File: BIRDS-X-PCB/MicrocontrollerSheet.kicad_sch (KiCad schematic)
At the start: 10 parts, among them J401 Conn_02x04_Odd_Even, J402 Conn_01x08, SW401 SW_Push, U401 STM32G031K8Tx, U402 MTT4B-Mini, U403 MT29F2G01ABAGDWB-IT-G_TR, Y401 ECS-2520SMV-080-FN-TR

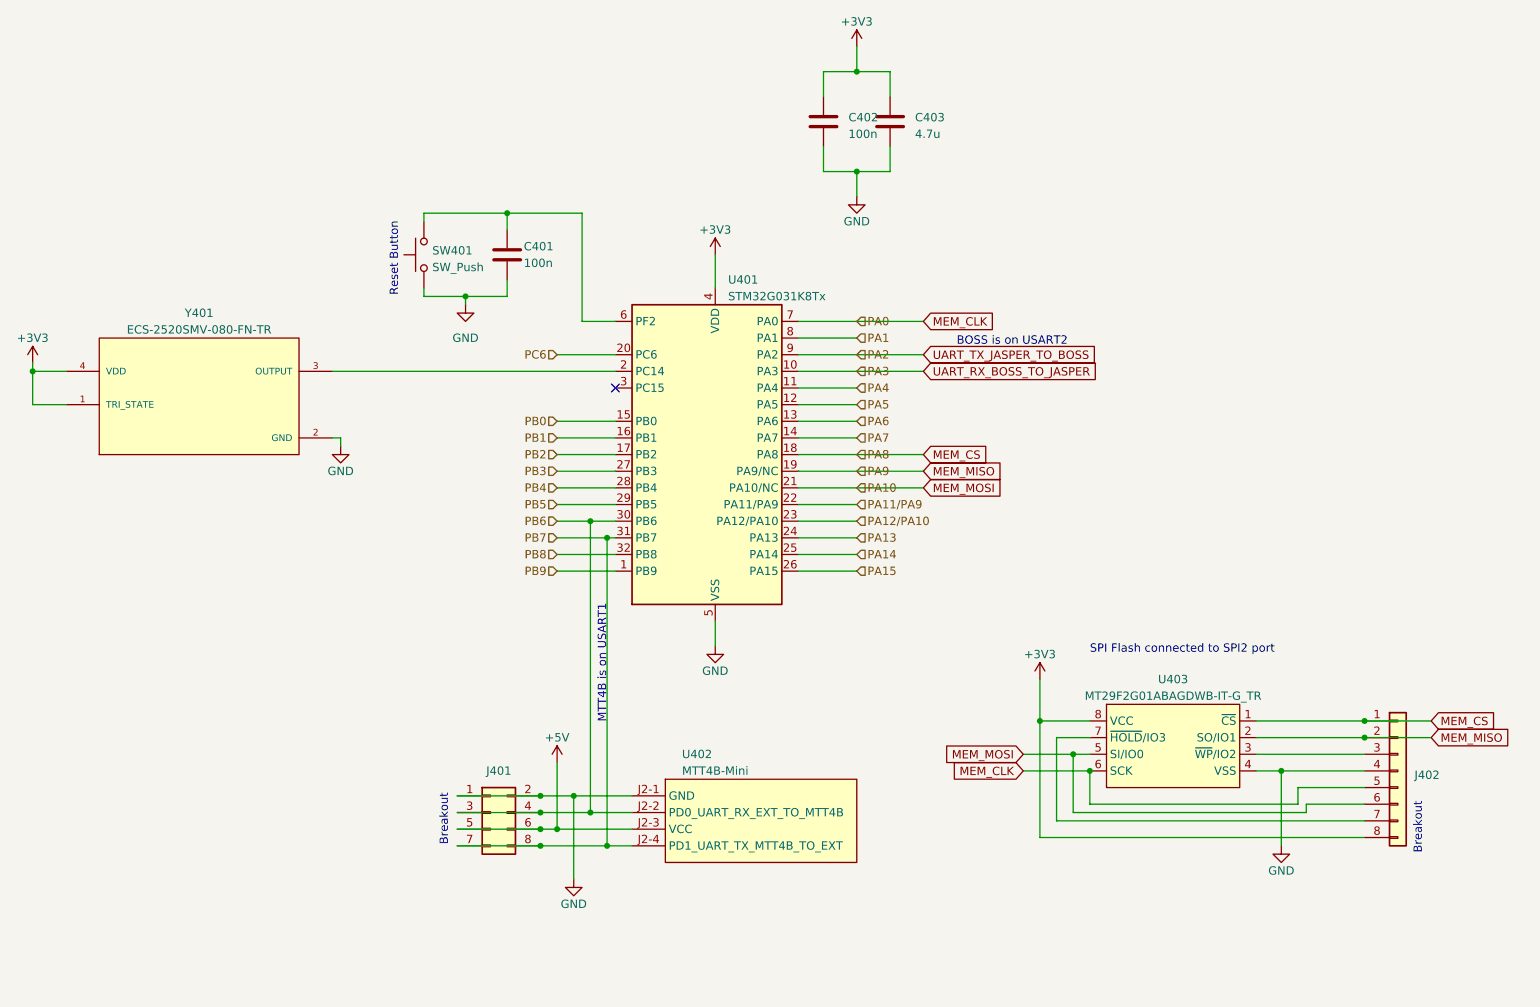
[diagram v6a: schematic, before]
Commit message: Semantic and symbol updates, begin review changes
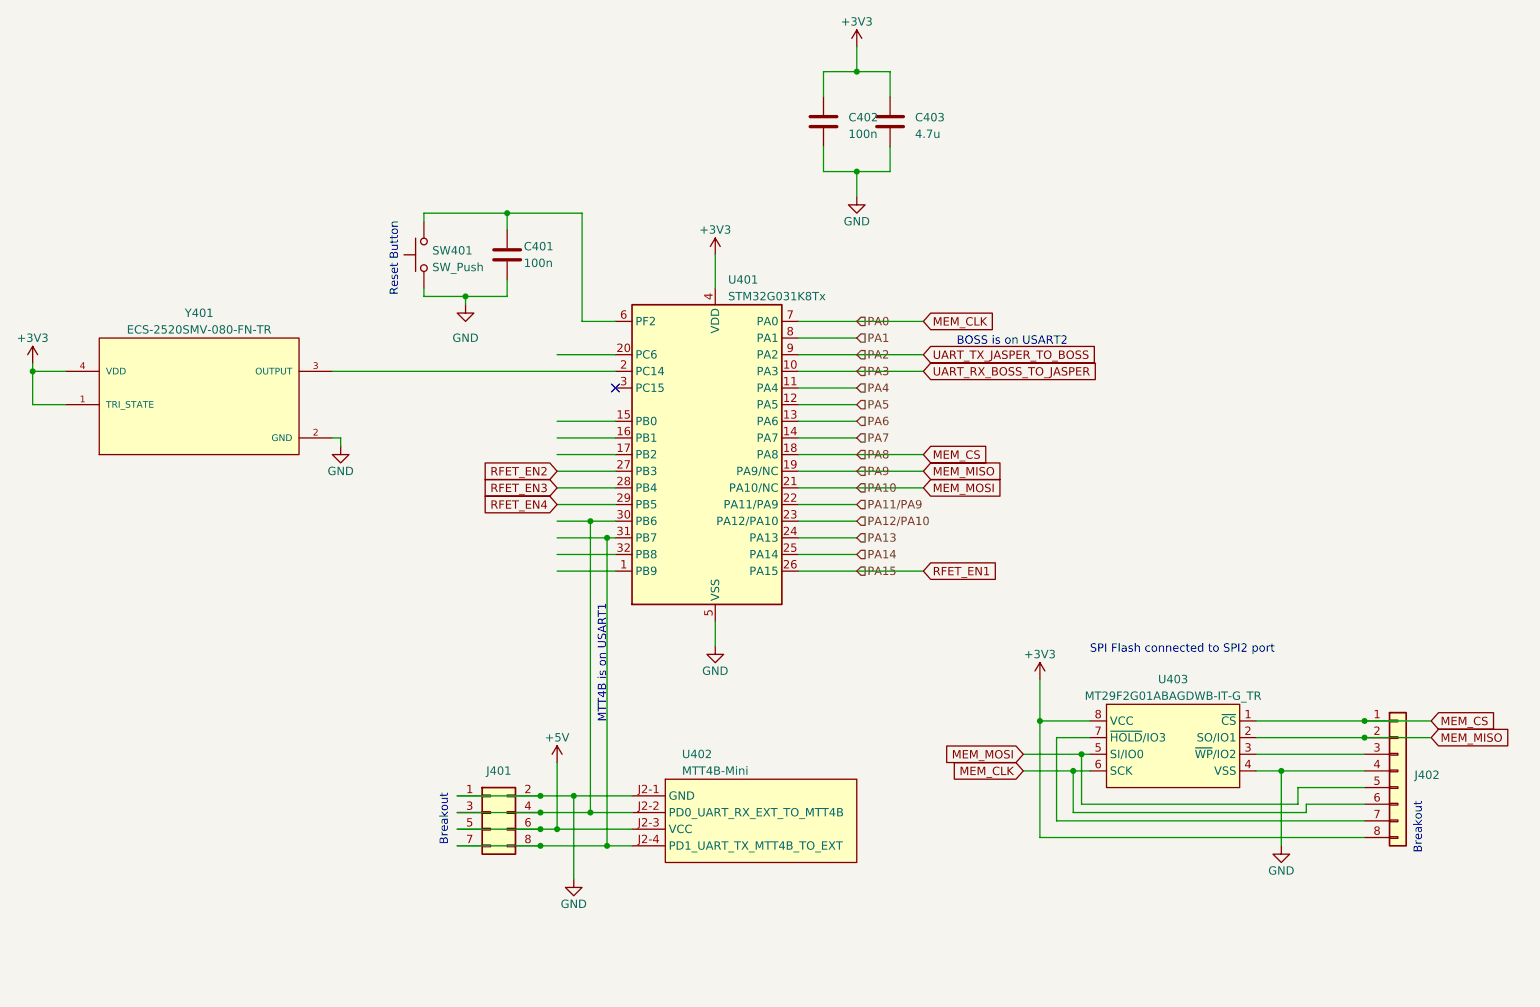
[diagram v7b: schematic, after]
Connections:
- net MEM_CLK: now also J402.6 (Pin_6); no longer J402.5 (Pin_5)
- net MEM_MOSI: now also J402.5 (Pin_5); no longer J402.6 (Pin_6)
- net PA15 renamed RFET_EN1
- net PB0: no longer names the net of U401.15 (PB0)
- net PB1: no longer names the net of U401.16 (PB1)
- net PB2: no longer names the net of U401.17 (PB2)
- net PB3 renamed RFET_EN2
- net PB4 renamed RFET_EN3
- net PB5 renamed RFET_EN4
- net PB6: no longer names the net of J401.3 (Pin_3), J401.4 (Pin_4), U401.30 (PB6), U402.J2-2 (PD0_UART_RX_EXT_TO_MTT4B)
- net PB7: no longer names the net of J401.7 (Pin_7), J401.8 (Pin_8), U401.31 (PB7), U402.J2-4 (PD1_UART_TX_MTT4B_TO_EXT)
- net PB8: no longer names the net of U401.32 (PB8)
- net PB9: no longer names the net of U401.1 (PB9)
- net PC6: no longer names the net of U401.20 (PC6)
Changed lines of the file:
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@@
 (kicad_sch (version 20230121) (generator eeschema)
   (paper "USLetter")
-  (junction (at 198.12 143.51) (diameter 0) (color 0 0 0 0)
-  )
   (junction (at 114.3 147.32) (diameter 0) (color 0 0 0 0)
   )
-  (junction (at 195.58 140.97) (diameter 0) (color 0 0 0 0)
-  )
   (junction (at 240.03 138.43) (diameter 0) (color 0 0 0 0)
   )
@@
   (junction (at 227.33 143.51) (diameter 0) (color 0 0 0 0)
   )
+  (junction (at 196.85 140.97) (diameter 0) (color 0 0 0 0)
+  )
   (junction (at 124.46 107.95) (diameter 0) (color 0 0 0 0)
   )
@@
   )
   (junction (at 36.83 82.55) (diameter 0) (color 0 0 0 0)
+  )
+  (junction (at 195.58 143.51) (diameter 0) (color 0 0 0 0)
   )
   (junction (at 114.3 149.86) (diameter 0) (color 0 0 0 0)
@@
     (stroke (width 0) (type default))
   )
-  (wire (pts (xy 153.67 113.03) (xy 162.56 113.03))
+  (wire (pts (xy 153.67 113.03) (xy 172.72 113.03))
     (stroke (width 0) (type default))
   )
@@
     (stroke (width 0) (type default))
   )
-  (wire (pts (xy 187.96 140.97) (xy 195.58 140.97))
-    (stroke (width 0) (type default))
-  )
   (wire (pts (xy 121.92 149.86) (xy 121.92 105.41))
     (stroke (width 0) (type default))
@@
     (stroke (width 0) (type default))
   )
+  (wire (pts (xy 196.85 140.97) (xy 196.85 148.59))
+    (stroke (width 0) (type default))
+  )
   (wire (pts (xy 119.38 147.32) (xy 128.27 147.32))
     (stroke (width 0) (type default))
@@
     (stroke (width 0) (type default))
   )
-  (wire (pts (xy 187.96 143.51) (xy 198.12 143.51))
+  (wire (pts (xy 187.96 143.51) (xy 195.58 143.51))
     (stroke (width 0) (type default))
   )
@@
     (stroke (width 0) (type default))
   )
+  (wire (pts (xy 196.85 140.97) (xy 198.12 140.97))
+    (stroke (width 0) (type default))
+  )
   (wire (pts (xy 153.67 97.79) (xy 172.72 97.79))
     (stroke (width 0) (type default))
@@
     (stroke (width 0) (type default))
   )
-  (wire (pts (xy 198.12 143.51) (xy 198.12 148.59))
-    (stroke (width 0) (type default))
-  )
   (wire (pts (xy 153.67 100.33) (xy 172.72 100.33))
     (stroke (width 0) (type default))
@@
     (stroke (width 0) (type default))
   )
-  (wire (pts (xy 198.12 148.59) (xy 229.87 148.59))
+  (wire (pts (xy 196.85 148.59) (xy 229.87 148.59))
+    (stroke (width 0) (type default))
+  )
+  (wire (pts (xy 195.58 143.51) (xy 195.58 149.86))
     (stroke (width 0) (type default))
   )
@@
     (stroke (width 0) (type default))
   )
+  (wire (pts (xy 195.58 143.51) (xy 198.12 143.51))
+    (stroke (width 0) (type default))
+  )
   (wire (pts (xy 101.6 154.94) (xy 114.3 154.94))
     (stroke (width 0) (type default))
@@
     (stroke (width 0) (type default))
   )
-  (wire (pts (xy 195.58 140.97) (xy 195.58 149.86))
-    (stroke (width 0) (type default))
-  )
   (wire (pts (xy 153.67 80.01) (xy 172.72 80.01))
     (stroke (width 0) (type default))
@@
     (stroke (width 0) (type default))
   )
-  (wire (pts (xy 198.12 140.97) (xy 195.58 140.97))
+  (wire (pts (xy 187.96 140.97) (xy 196.85 140.97))
     (stroke (width 0) (type default))
   )
@@
     )
   )
+  (global_label "RFET_EN3" (shape input) (at 116.84 100.33 180) (fields_autoplaced)
+    (effects (font (size 1.27 1.27)) (justify right))
+    (property "Intersheetrefs" "${INTERSHEET_REFS}" (at 104.8024 100.33 0)
+      (effects (font (size 1.27 1.27)) (justify right) hide)
+    )
+  )
   (global_label "UART_RX_BOSS_TO_JASPER" (shape input) (at 172.72 82.55 0) (fields_autoplaced)
     (effects (font (size 1.27 1.27)) (justify left))
     (property "Intersheetrefs" "${INTERSHEET_REFS}" (at 200.9047 82.55 0)
+      (effects (font (size 1.27 1.27)) (justify left) hide)
+    )
+  )
+  (global_label "RFET_EN1" (shape input) (at 172.72 113.03 0) (fields_autoplaced)
+    (effects (font (size 1.27 1.27)) (justify left))
+    (property "Intersheetrefs" "${INTERSHEET_REFS}" (at 184.7576 113.03 0)
       (effects (font (size 1.27 1.27)) (justify left) hide)
     )
@@
     )
   )
+  (global_label "RFET_EN2" (shape input) (at 116.84 97.79 180) (fields_autoplaced)
+    (effects (font (size 1.27 1.27)) (justify right))
+    (property "Intersheetrefs" "${INTERSHEET_REFS}" (at 104.8024 97.79 0)
+      (effects (font (size 1.27 1.27)) (justify right) hide)
+    )
+  )
+  (global_label "RFET_EN4" (shape input) (at 116.84 102.87 180) (fields_autoplaced)
+    (effects (font (size 1.27 1.27)) (justify right))
+    (property "Intersheetrefs" "${INTERSHEET_REFS}" (at 104.8024 102.87 0)
+      (effects (font (size 1.27 1.27)) (justify right) hide)
+    )
+  )
   (global_label "MEM_MISO" (shape input) (at 250.19 138.43 0) (fields_autoplaced)
     (effects (font (size 1.27 1.27)) (justify left))
@@
     )
   )
-  (hierarchical_label "PC6" (shape input) (at 116.84 80.01 180) (fields_autoplaced)
-    (effects (font (size 1.27 1.27)) (justify right))
-  )
-  (hierarchical_label "PB0" (shape input) (at 116.84 90.17 180) (fields_autoplaced)
-    (effects (font (size 1.27 1.27)) (justify right))
-  )
   (hierarchical_label "PA2" (shape input) (at 162.56 80.01 0) (fields_autoplaced)
     (effects (font (size 1.27 1.27)) (justify left))
   )
-  (hierarchical_label "PB8" (shape input) (at 116.84 110.49 180) (fields_autoplaced)
-    (effects (font (size 1.27 1.27)) (justify right))
-  )
-  (hierarchical_label "PB3" (shape input) (at 116.84 97.79 180) (fields_autoplaced)
-    (effects (font (size 1.27 1.27)) (justify right))
-  )
   (hierarchical_label "PA3" (shape input) (at 162.56 82.55 0) (fields_autoplaced)
     (effects (font (size 1.27 1.27)) (justify left))
@@
     (effects (font (size 1.27 1.27)) (justify left))
   )
-  (hierarchical_label "PB2" (shape input) (at 116.84 95.25 180) (fields_autoplaced)
-    (effects (font (size 1.27 1.27)) (justify right))
-  )
   (hierarchical_label "PA7" (shape input) (at 162.56 92.71 0) (fields_autoplaced)
     (effects (font (size 1.27 1.27)) (justify left))
   )
-  (hierarchical_label "PB1" (shape input) (at 116.84 92.71 180) (fields_autoplaced)
-    (effects (font (size 1.27 1.27)) (justify right))
-  )
   (hierarchical_label "PA11{slash}PA9" (shape input) (at 162.56 102.87 0) (fields_autoplaced)
     (effects (font (size 1.27 1.27)) (justify left))
@@
     (effects (font (size 1.27 1.27)) (justify left))
   )
-  (hierarchical_label "PB6" (shape input) (at 116.84 105.41 180) (fields_autoplaced)
-    (effects (font (size 1.27 1.27)) (justify right))
-  )
   (hierarchical_label "PA0" (shape input) (at 162.56 74.93 0) (fields_autoplaced)
     (effects (font (size 1.27 1.27)) (justify left))
@@
     (effects (font (size 1.27 1.27)) (justify left))
   )
-  (hierarchical_label "PB4" (shape input) (at 116.84 100.33 180) (fields_autoplaced)
-    (effects (font (size 1.27 1.27)) (justify right))
-  )
   (hierarchical_label "PA5" (shape input) (at 162.56 87.63 0) (fields_autoplaced)
     (effects (font (size 1.27 1.27)) (justify left))
@@
     (effects (font (size 1.27 1.27)) (justify left))
   )
-  (hierarchical_label "PB7" (shape input) (at 116.84 107.95 180) (fields_autoplaced)
-    (effects (font (size 1.27 1.27)) (justify right))
-  )
   (hierarchical_label "PA15" (shape input) (at 162.56 113.03 0) (fields_autoplaced)
     (effects (font (size 1.27 1.27)) (justify left))
   )
-  (hierarchical_label "PB9" (shape input) (at 116.84 113.03 180) (fields_autoplaced)
-    (effects (font (size 1.27 1.27)) (justify right))
-  )
   (hierarchical_label "PA12{slash}PA10" (shape input) (at 162.56 105.41 0) (fields_autoplaced)
     (effects (font (size 1.27 1.27)) (justify left))
@@
     (effects (font (size 1.27 1.27)) (justify left))
   )
-  (hierarchical_label "PB5" (shape input) (at 116.84 102.87 180) (fields_autoplaced)
-    (effects (font (size 1.27 1.27)) (justify right))
-  )
   (symbol (lib_id "power:GND") (at 227.33 154.94 0) (unit 1)

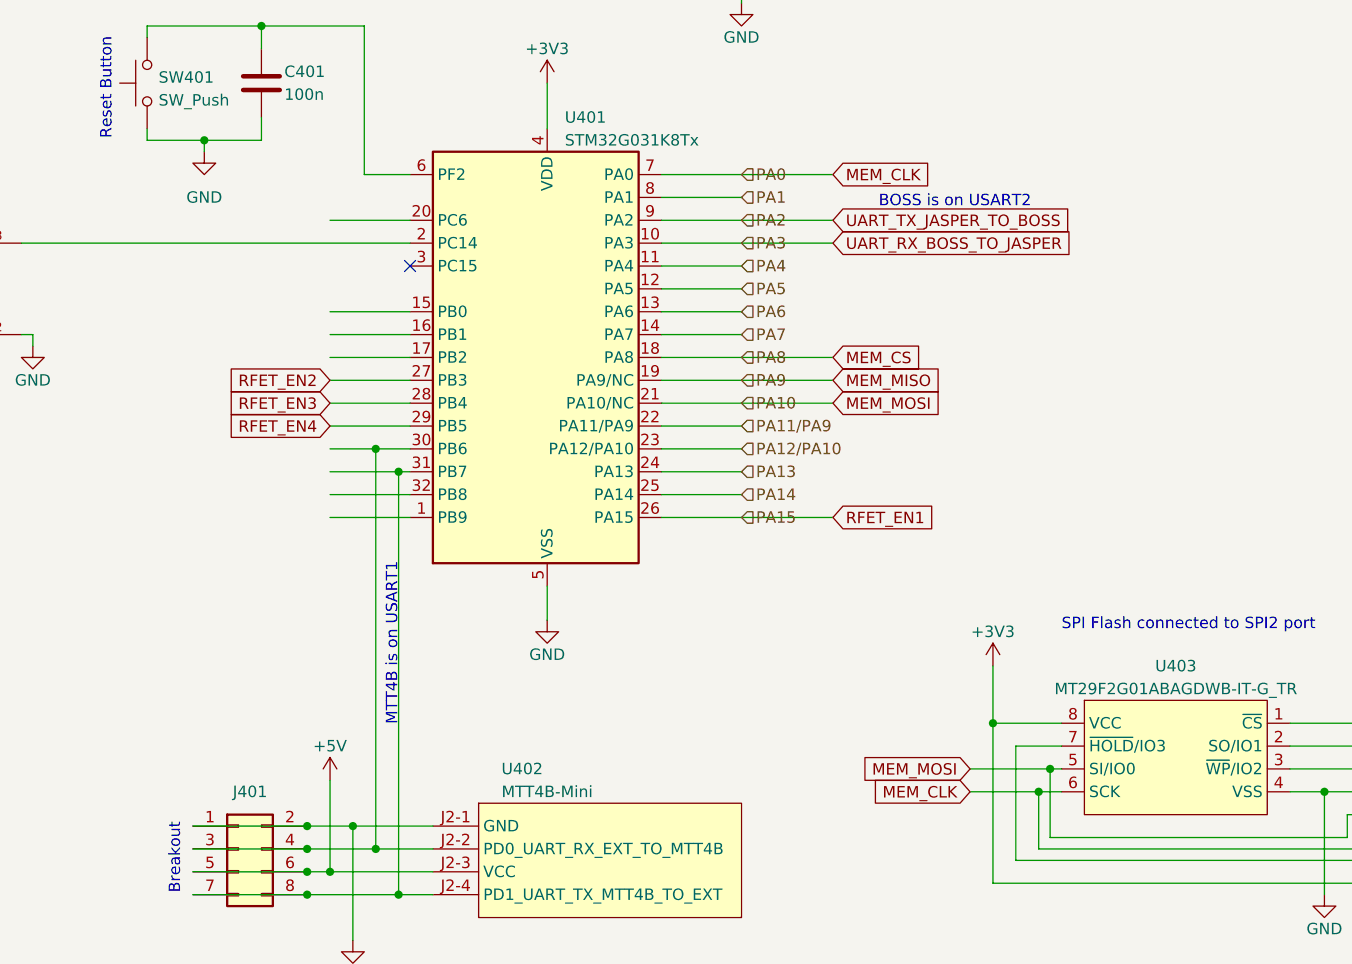
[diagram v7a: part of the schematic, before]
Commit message: MCU pin assignment review
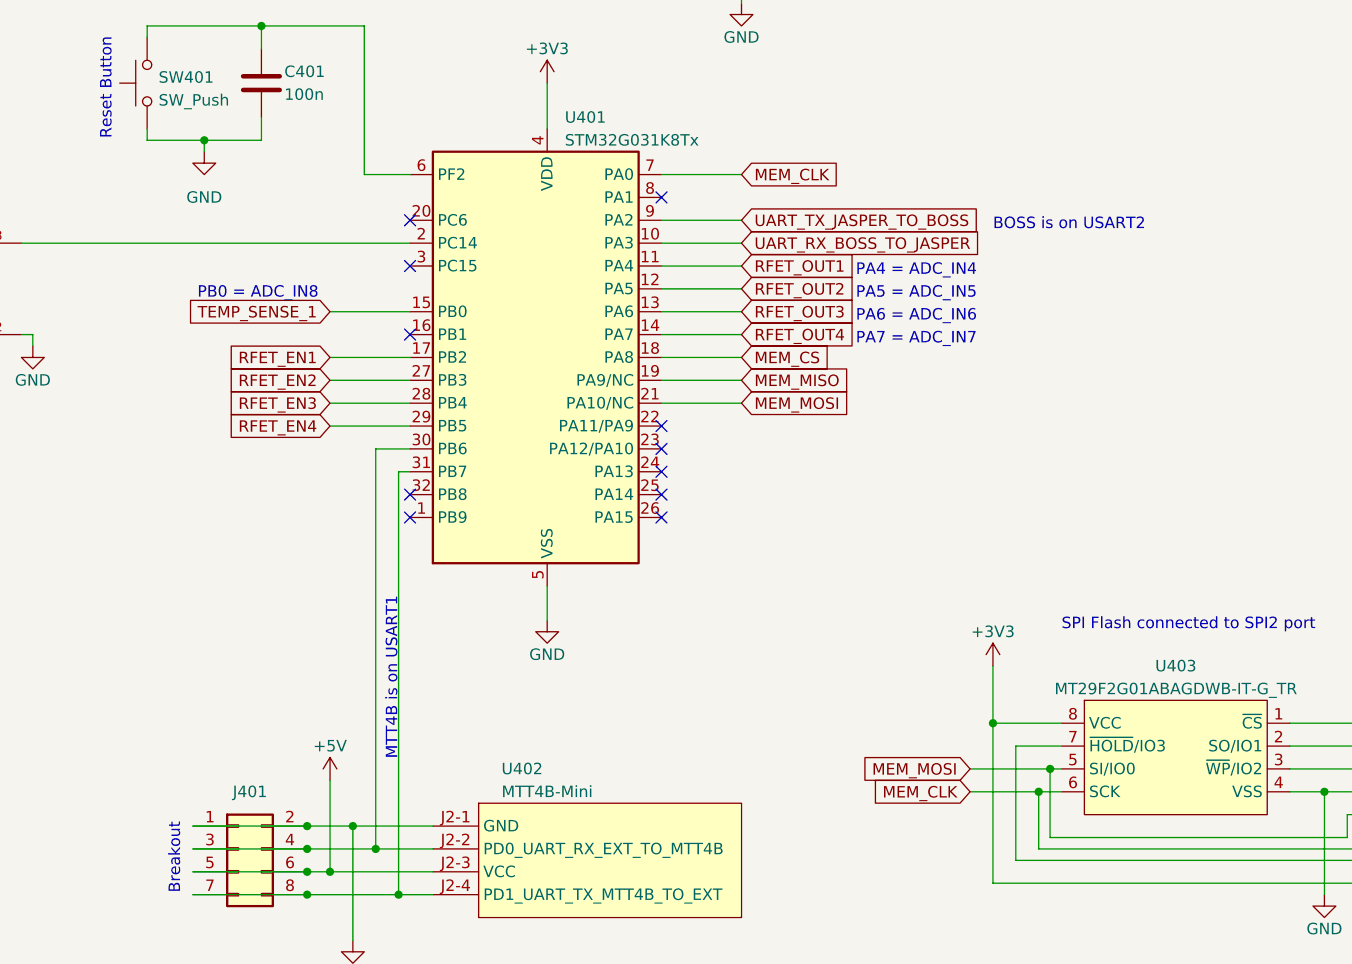
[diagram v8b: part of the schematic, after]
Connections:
- net RFET_EN1: now also U401.17 (PB2); no longer U401.26 (PA15)
- net TEMP_SENSE_1: now reaches U401.15 (PB0)
- net PA1: no longer names the net of U401.8 (PA1)
- net PA11/PA9: no longer names the net of U401.22 (PA11/PA9)
- net PA12/PA10: no longer names the net of U401.23 (PA12/PA10)
- net PA13: no longer names the net of U401.24 (PA13)
- net PA14: no longer names the net of U401.25 (PA14)
- net PA4 renamed RFET_OUT1
- net PA5 renamed RFET_OUT2
- net PA6 renamed RFET_OUT3
- net PA7 renamed RFET_OUT4
- no-connect marks 1 -> 11
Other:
- note added: "PA4 = ADC_IN4"
- note added: "PA5 = ADC_IN5"
- note added: "PA6 = ADC_IN6"
- note added: "PA7 = ADC_IN7"
- note added: "PB0 = ADC_IN8"
